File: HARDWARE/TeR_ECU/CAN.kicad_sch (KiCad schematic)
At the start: 10 parts, among them U5 TCAN332

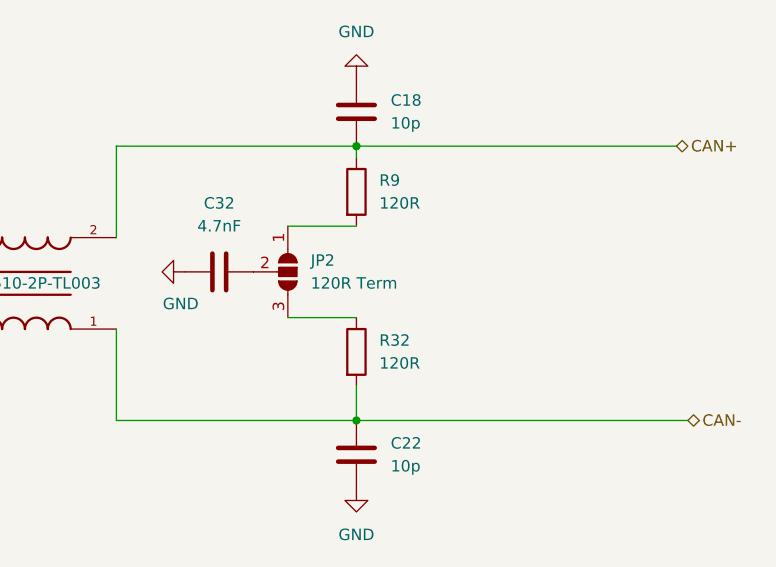
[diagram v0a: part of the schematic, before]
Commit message: Added eeprom lib inc path and fixed 120R resistors in Hardware
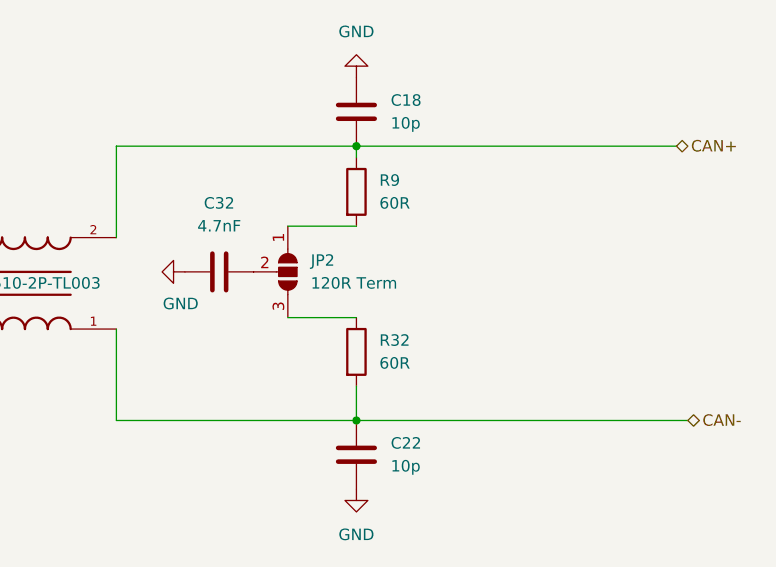
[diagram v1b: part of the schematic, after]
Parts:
- R32, R9: value 120R -> 60R
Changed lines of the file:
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@@
 		(shape output)
 		(at 80.01 92.71 180)
-		(fields_autoplaced yes)
 		(effects
 			(font
@@
 		(shape bidirectional)
 		(at 219.71 80.01 0)
-		(fields_autoplaced yes)
 		(effects
 			(font
@@
 		(shape bidirectional)
 		(at 220.98 110.49 0)
-		(fields_autoplaced yes)
 		(effects
 			(font
@@
 		(shape input)
 		(at 80.01 90.17 180)
-		(fields_autoplaced yes)
 		(effects
 			(font
@@
 			)
 		)
-		(property "Value" "120R"
+		(property "Value" "60R"
 			(at 186.69 86.3599 0)
 			(effects
@@
 			)
 		)
-		(property "Value" "120R"
+		(property "Value" "60R"
 			(at 186.69 104.1399 0)
 			(effects
